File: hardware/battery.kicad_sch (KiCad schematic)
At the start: 33 parts, among them J2 B2B-XH-A, J3 PRPC001DAAN-RC, Q1 DMG2305UX-7, Q2 DMN2005, Q3 DMN2005, U2 BQ29728DSER, U3 MCP73833T-FCI/MF

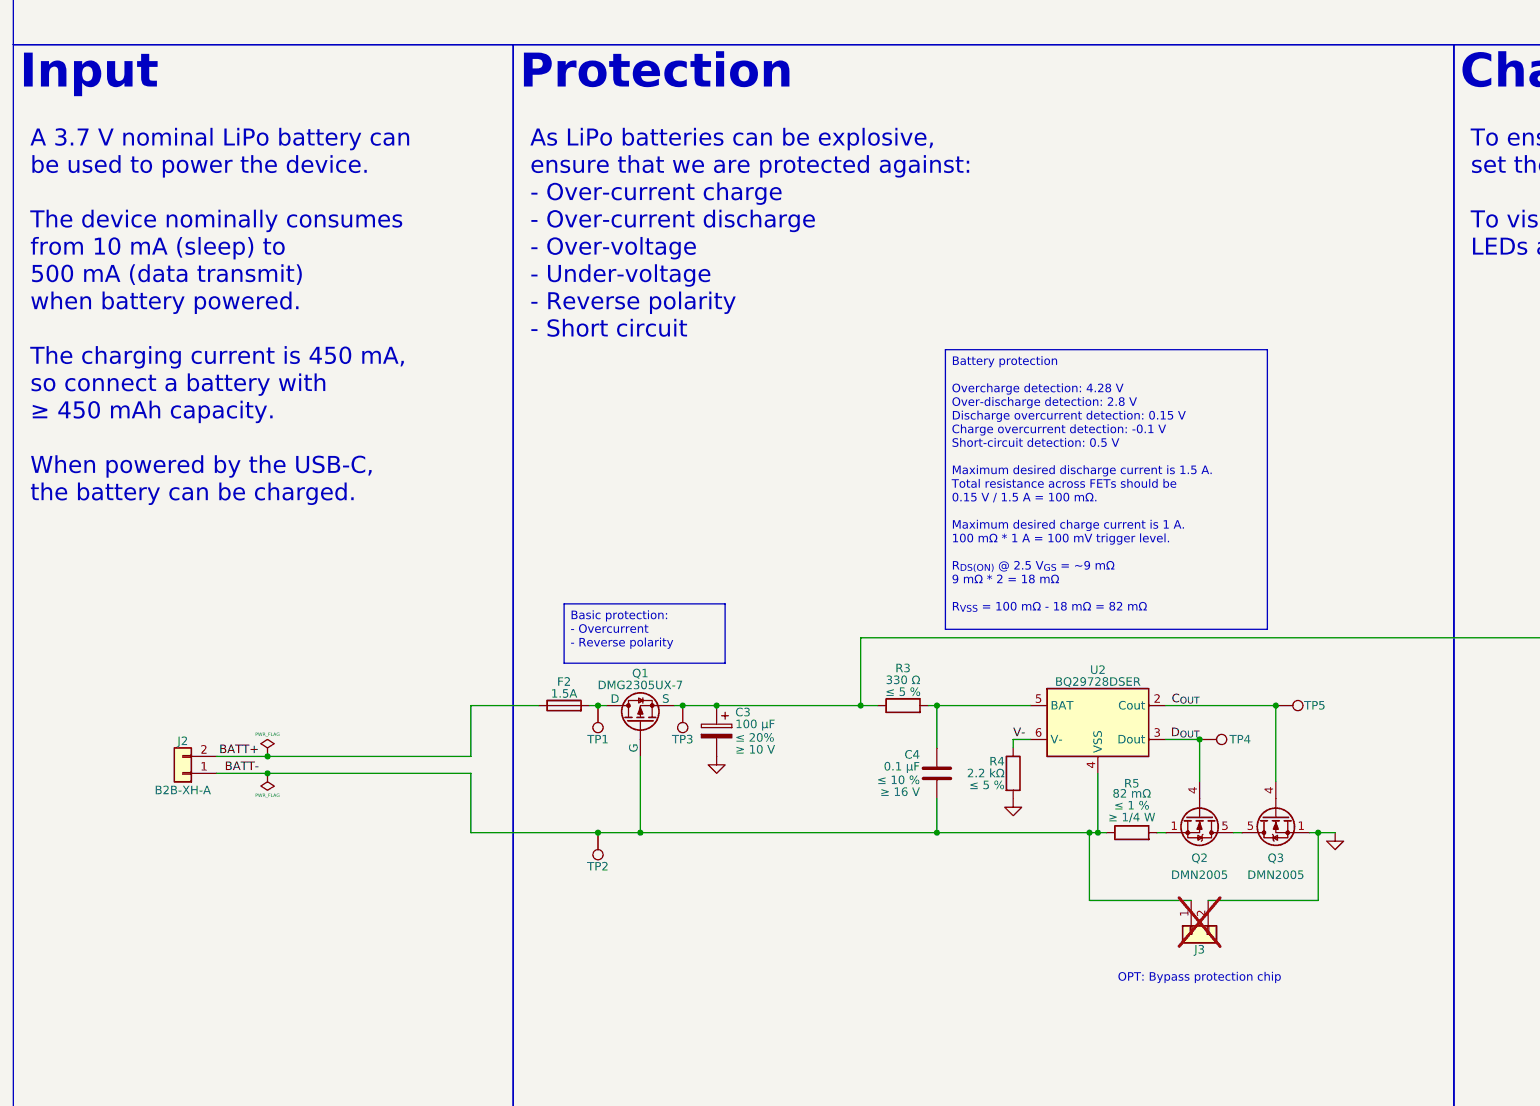
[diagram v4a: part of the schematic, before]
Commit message: HW: Unused GPIOs to headers, refine schematics
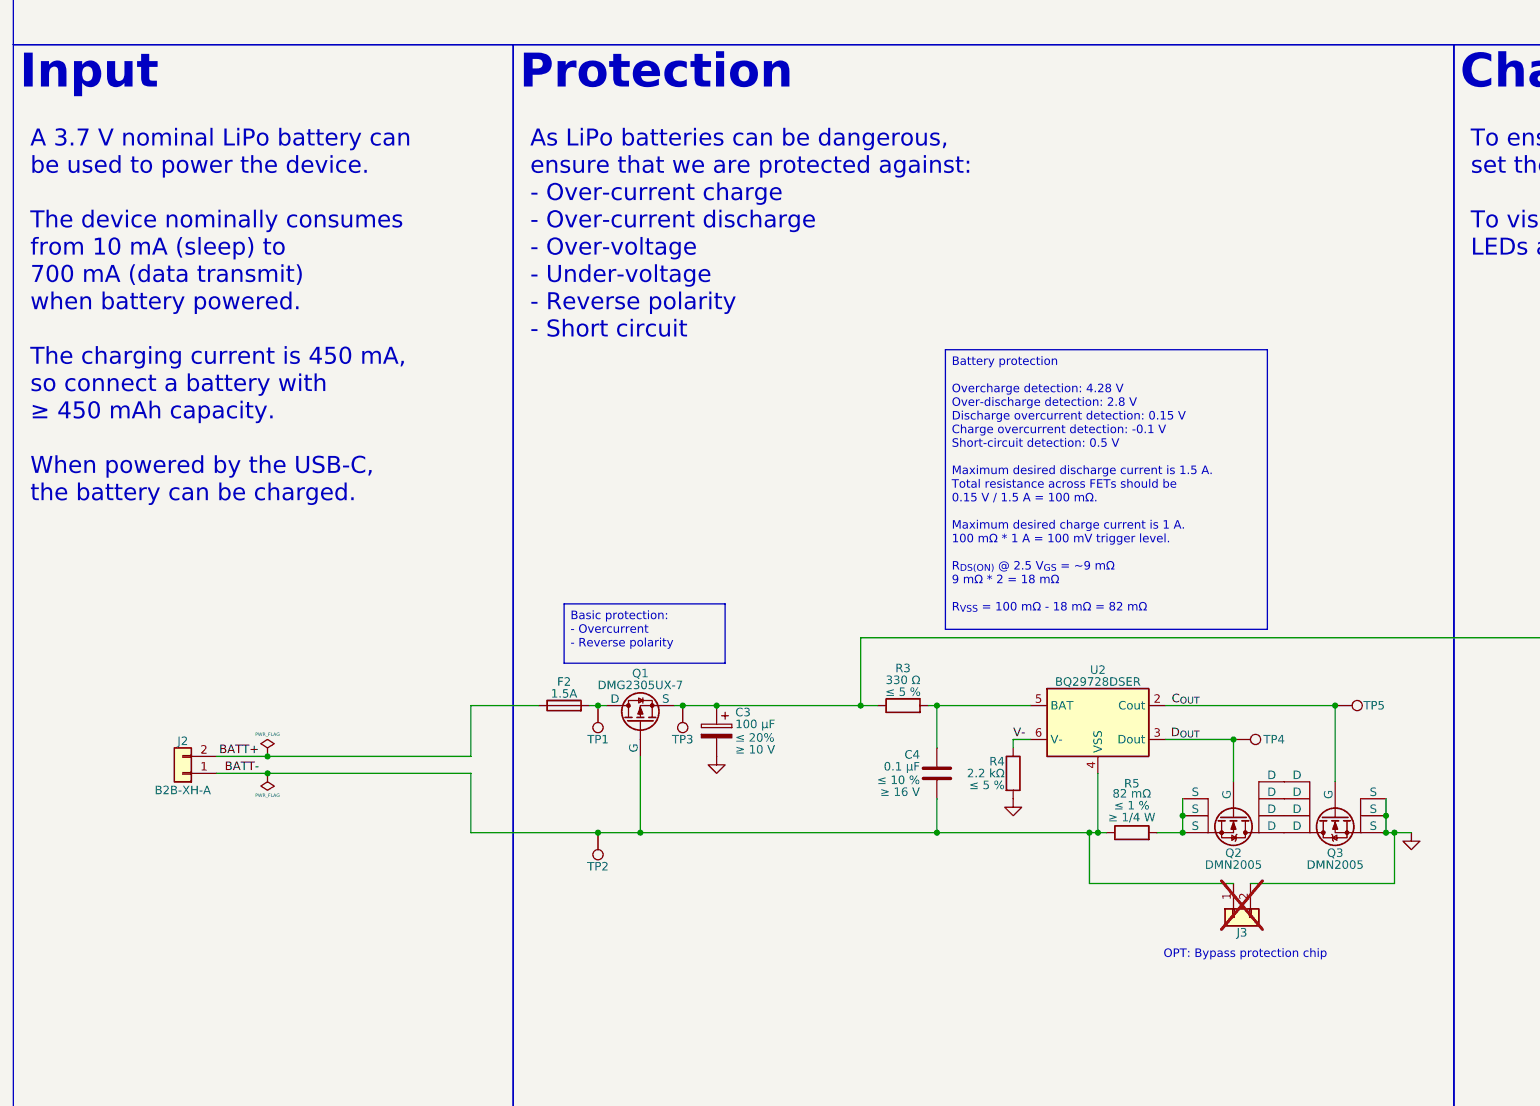
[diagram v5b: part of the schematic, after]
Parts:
- removed Q3: DMN2005, Package_SON:Diodes_PowerDI3333-8, symbol Transistor_FET:DMN3008SFG
- added Q3: DMN2005, Package_SON:Diodes_PowerDI3333-8, symbol PowerFET:Q_NMOS_PowerDI333-8
- Q2: symbol Transistor_FET:DMN3008SFG -> PowerFET:Q_NMOS_PowerDI333-8
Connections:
- net C_{OUT}: now also Q3.4 (G)
- net GND: now also Q3.1 (S), Q3.2 (S), Q3.3 (S)
- net at Q2.5 (D): now also Q3.5 (D)
- new net: Q2.6 (D), Q3.6 (D)
- new net: Q2.7 (D), Q3.7 (D)
- new net: Q2.8 (D), Q3.8 (D)
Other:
- note added: "A 3.7 V nominal LiPo battery can be used to power the device. The device nominally consumes from 10 mA (sleep) to 700 mA (data transmit) when battery powered. The charging current is 450 mA, so connect a battery with ≥ 450 mAh capacity. When powered by the USB-C, the battery can be charged."
- note added: "As LiPo batteries can be dangerous, ensure that we are protected against: - Over-current charge - Over-current discharge - Over-voltage - Under-voltage - Reverse polarity - Short circuit"
- note removed: "A 3.7 V nominal LiPo battery can be used to power the device. The device nominally consumes from 10 mA (sleep) to 500 mA (data transmit) when battery powered. The charging current is 450 mA, so connect a battery with ≥ 450 mAh capacity. When powered by the USB-C, the battery can be charged."
- note removed: "As LiPo batteries can be explosive, ensure that we are protected against: - Over-current charge - Over-current discharge - Over-voltage - Under-voltage - Reverse polarity - Short circuit"
- moved on the sheet: J3, TP4, TP5

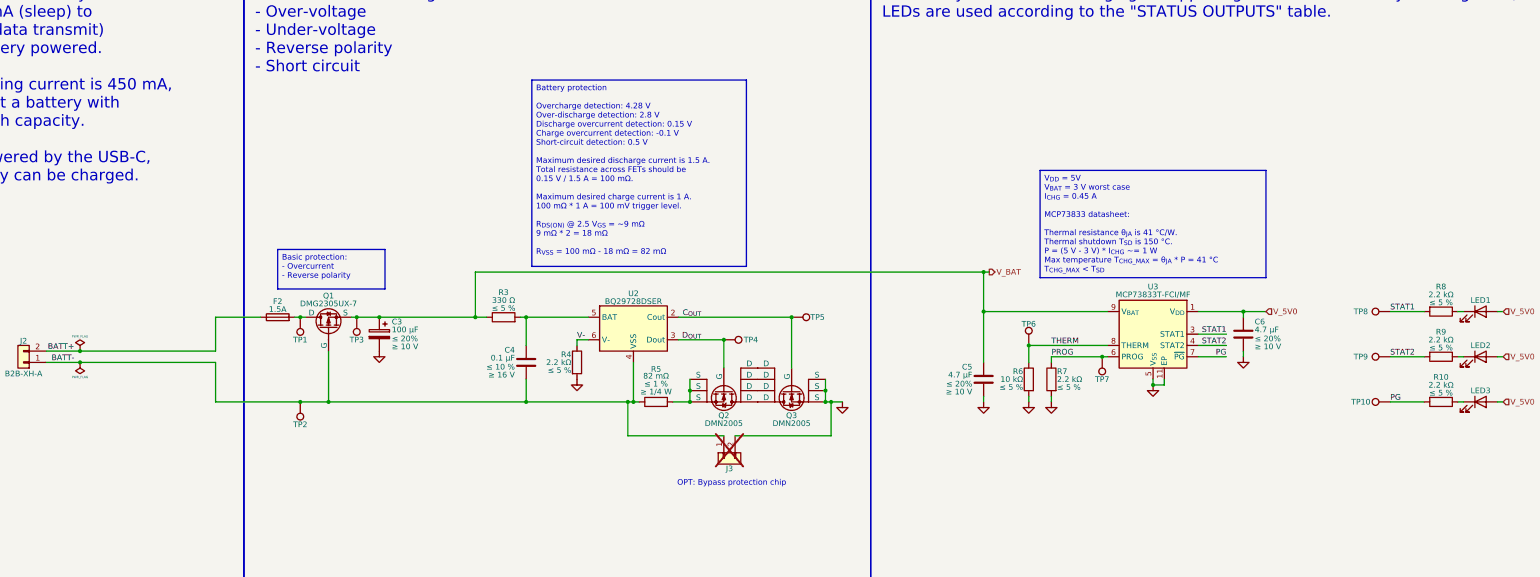
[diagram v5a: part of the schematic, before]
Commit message: HW: Refine BOM, add comments, color code power rails
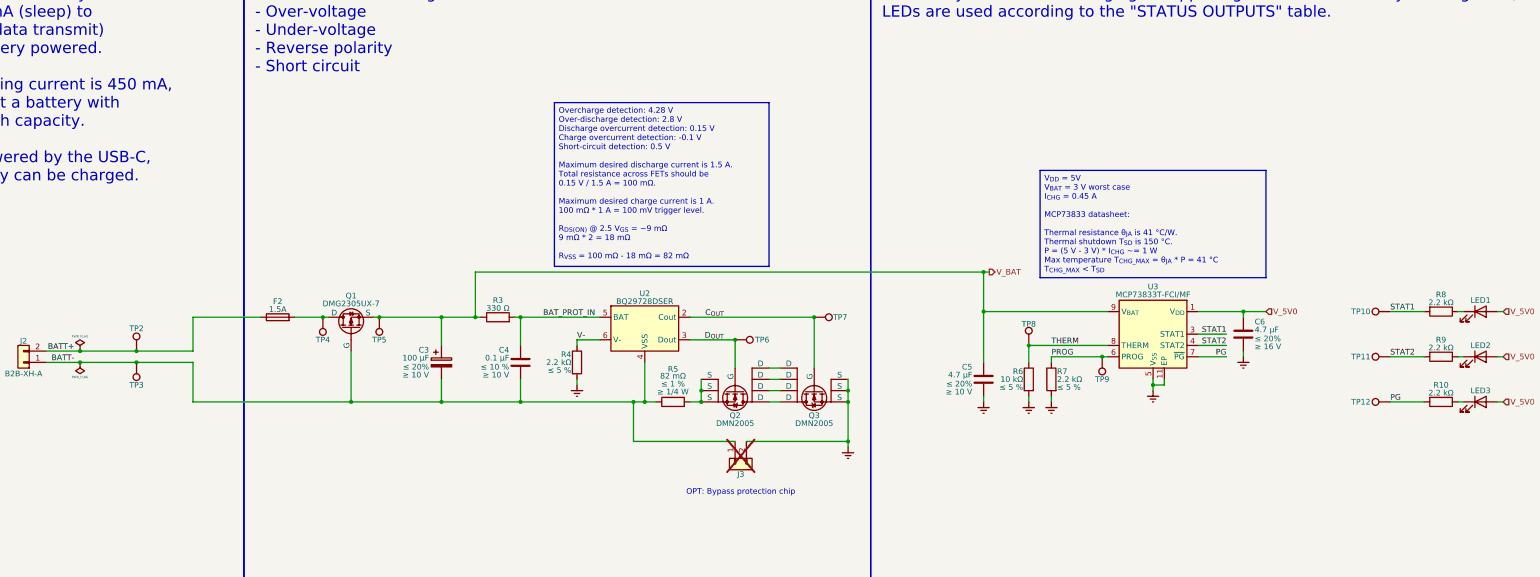
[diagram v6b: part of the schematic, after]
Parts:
- added TP2: TestPoint, TestPoint:TestPoint_Pad_D1.0mm, symbol Connector:TestPoint
- C3: Class AlumElec -> (none); Size 5.0mmx2.0mm -> (none)
- C4: Voltage ≥ 16 V -> ≥ 10 V
- C5: footprint Capacitor_SMD:C_0402_1005Metric -> Capacitor_SMD:C_0603_1608Metric; DigiKey Part Number 490-14306-1-ND -> 490-7203-1-ND; MPN GRM155R61A475MEAAD -> GRM188R61E475KE11D
- C6: footprint Capacitor_SMD:C_0402_1005Metric -> Capacitor_SMD:C_0603_1608Metric; DigiKey Part Number 490-14306-1-ND -> 490-7203-1-ND; MPN GRM155R61A475MEAAD -> GRM188R61E475KE11D; Size 0402 -> 0603; Voltage ≥ 10 V -> ≥ 16 V
- R10, R8, R9: Tolerance ≤ 5 % -> ≤ 10 %
- TP10: renamed from TP8; now left out of the parts list
- TP11: renamed from TP9; now left out of the parts list
- TP12: renamed from TP10; now left out of the parts list
- TP3: renamed from TP2; now left out of the parts list
- TP4: renamed from TP1; now left out of the parts list
- TP5: renamed from TP3; now left out of the parts list
- TP6: renamed from TP4; now left out of the parts list
- TP7: renamed from TP5; now left out of the parts list
- TP8: renamed from TP6; now left out of the parts list
- TP9: renamed from TP7; now left out of the parts list
- U3: Footprint review check (none) -> +
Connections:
- net BATT+: now also TP2.1
- net BATT-: now also C3.2
- net GND: no longer C3.2
- net BAT_PROT_IN: now reaches C4.1, R3.2, U2.5 (BAT)
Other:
- moved on the sheet: C3, C4, J3, Q1, Q2, Q3, R3, R5, TP3, TP4, TP5, TP6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

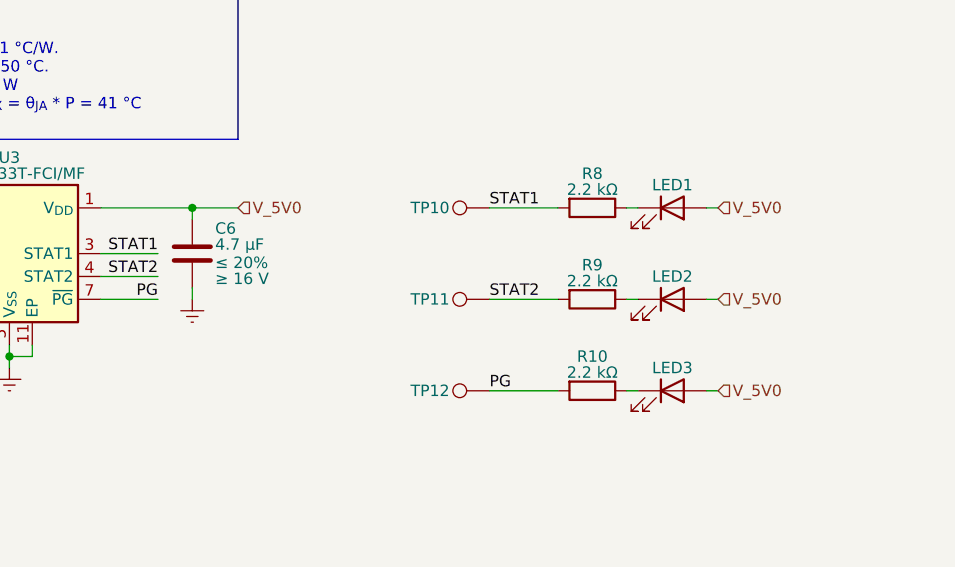
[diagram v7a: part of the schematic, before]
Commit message: HW: Add global symbols for V_BAT and V_5V0
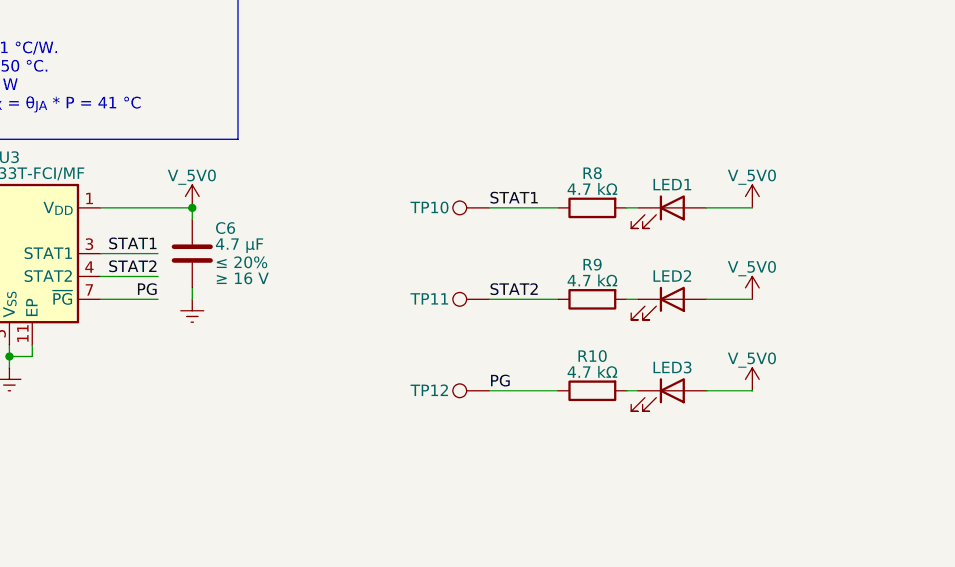
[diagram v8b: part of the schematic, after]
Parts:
- R10, R8, R9: value 2.2 kΩ -> 4.7 kΩ; DigiKey Part Number 732-560112110087CT-ND -> 732-560112110245CT-ND; MPN 560112110087 -> 560112110245; Tolerance ≤ 10 % -> ≤ 5 %
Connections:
- net PG: now also R10.1; no longer R10.2
- net STAT1: now also R8.1; no longer R8.2
- net STAT2: now also R9.1; no longer R9.2
- net at LED1.1 (K): now also R8.2; no longer R8.1
- net at LED2.1 (K): now also R9.2; no longer R9.1
- net at LED3.1 (K): now also R10.2; no longer R10.1
